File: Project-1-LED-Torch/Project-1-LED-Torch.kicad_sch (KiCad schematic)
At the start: 0 parts

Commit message: do schematic design, step 2, add symbols
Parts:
- added BT1: Battery_Cell, symbol Device:Battery_Cell
- added D1: LED, symbol Device:LED
- added R1: R, symbol Device:R
- added SW1: SW_DPDT_x2, symbol Switch:SW_DPDT_x2

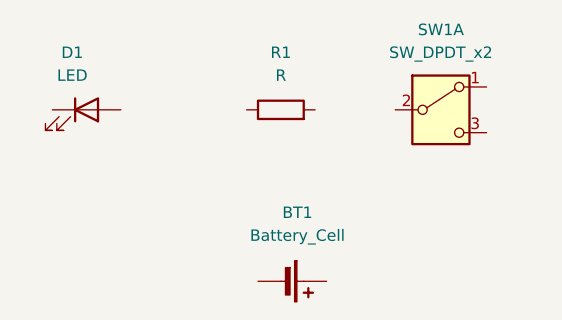
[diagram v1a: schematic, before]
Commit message: bugfix schematic design, step 2, change symbol
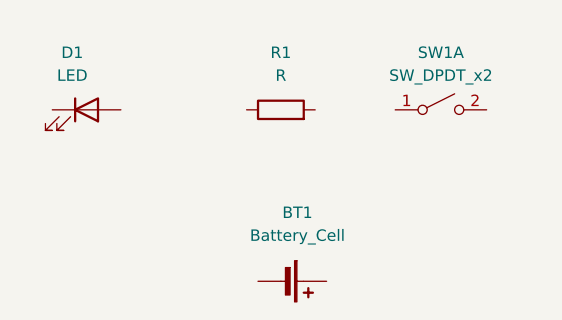
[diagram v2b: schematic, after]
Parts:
- SW1: symbol Switch:SW_DPDT_x2 -> Switch:SW_DPST_x2
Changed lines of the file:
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@@
 	)
 	(symbol
-		(lib_id "Switch:SW_DPDT_x2")
+		(lib_id "Switch:SW_DPST_x2")
 		(at 148.59 76.2 0)
 		(unit 1)
@@
 		(fields_autoplaced yes)
 		(property "Reference" "SW1"
-			(at 148.59 67.31 0)
+			(at 148.59 69.85 0)
 			(show_name no)
 			(do_not_autoplace no)
@@
 		)
 		(property "Value" "SW_DPDT_x2"
-			(at 148.59 69.85 0)
+			(at 148.59 72.39 0)
 			(show_name no)
 			(do_not_autoplace no)
@@
 			)
 		)
-		(property "Description" "Switch, dual pole double throw, separate symbols"
+		(property "Description" "Single Pole Single Throw (SPST) switch, separate symbol"
 			(at 148.59 76.2 0)
 			(hide yes)
@@
 			)
 		)
-		(pin "6"
-		)
-		(pin "5"
-		)
 		(pin "4"

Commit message: do schematic design, step 3, arrange, annotate, associate footprints
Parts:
- BT1: footprint (none) -> Battery:BatteryHolder_Keystone_1058_1x2032
- D1: footprint (none) -> LED_THT:LED_D5.0mm
- R1: footprint (none) -> Resistor_THT:R_Axial_DIN0204_L3.6mm_D1.6mm_P7.62mm_Horizontal
- SW1: footprint (none) -> Button_Switch_THT:SW_TH_Tactile_Omron_B3F-100x
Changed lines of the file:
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@@
 			)
 		)
-		(property "Footprint" ""
+		(property "Footprint" "Resistor_THT:R_Axial_DIN0204_L3.6mm_D1.6mm_P7.62mm_Horizontal"
 			(at 130.81 77.978 90)
 			(hide yes)
@@
 			)
 		)
-		(property "Footprint" ""
+		(property "Footprint" "LED_THT:LED_D5.0mm"
 			(at 109.22 76.2 0)
 			(hide yes)
@@
 			)
 		)
-		(property "Footprint" ""
+		(property "Footprint" "Button_Switch_THT:SW_TH_Tactile_Omron_B3F-100x"
 			(at 148.59 76.2 0)
 			(hide yes)
@@
 			)
 		)
-		(property "Footprint" ""
+		(property "Footprint" "Battery:BatteryHolder_Keystone_1058_1x2032"
 			(at 132.334 95.25 90)
 			(hide yes)

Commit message: do schematic design, step 4, wiring
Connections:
- net at R1.1: now also D1.2 (A)
- net at R1.2: now also SW1.1 (A)
- net at D1.1 (K): now also BT1.2 (-)
- net at SW1.2 (B): now also BT1.1 (+)
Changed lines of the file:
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@@
 		(company "Jupiter SW")
+	)
+	(wire
+		(pts
+			(xy 134.62 76.2) (xy 143.51 76.2)
+		)
+		(stroke
+			(width 0)
+			(type default)
+		)
+	)
+	(wire
+		(pts
+			(xy 113.03 76.2) (xy 127 76.2)
+		)
+		(stroke
+			(width 0)
+			(type default)
+		)
+	)
+	(wire
+		(pts
+			(xy 101.6 76.2) (xy 101.6 95.25)
+		)
+		(stroke
+			(width 0)
+			(type default)
+		)
+	)
+	(wire
+		(pts
+			(xy 160.02 95.25) (xy 160.02 76.2)
+		)
+		(stroke
+			(width 0)
+			(type default)
+		)
+	)
+	(wire
+		(pts
+			(xy 105.41 76.2) (xy 101.6 76.2)
+		)
+		(stroke
+			(width 0)
+			(type default)
+		)
+	)
+	(wire
+		(pts
+			(xy 160.02 76.2) (xy 153.67 76.2)
+		)
+		(stroke
+			(width 0)
+			(type default)
+		)
+	)
+	(wire
+		(pts
+			(xy 101.6 95.25) (xy 128.27 95.25)
+		)
+		(stroke
+			(width 0)
+			(type default)
+		)
+	)
+	(wire
+		(pts
+			(xy 135.89 95.25) (xy 160.02 95.25)
+		)
+		(stroke
+			(width 0)
+			(type default)
+		)
 	)
 	(symbol
